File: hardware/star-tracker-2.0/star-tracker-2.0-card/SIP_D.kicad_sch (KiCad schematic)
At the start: 5 parts, among them J6 Conn_01x02, U7 OSD3358-512M-BSM

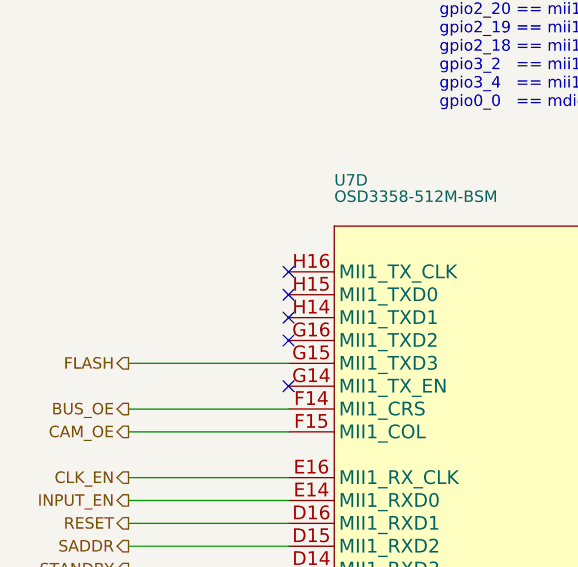
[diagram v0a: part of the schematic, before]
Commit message: Added IMU
added IMU, and i2c pull up resistors to schematic.
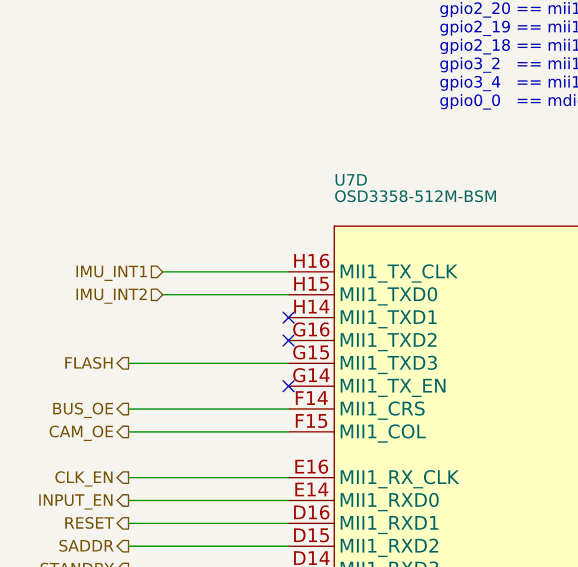
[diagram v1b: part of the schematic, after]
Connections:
- net IMU_INT2: now reaches U7.H15 (MII1_TXD0)
- net IMU_INT1: now reaches U7.H16 (MII1_TX_CLK)
- no-connect marks 20 -> 18
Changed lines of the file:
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@@
-	)
-	(no_connect
-		(at 127 116.84)
 	)
 	(no_connect
@@
 	)
 	(no_connect
-		(at 127 119.38)
-	)
-	(no_connect
 		(at 127 129.54)
 	)
@@
 	(wire
 		(pts
+			(xy 113.03 119.38) (xy 127 119.38)
+		)
+		(stroke
+			(width 0)
+			(type default)
+		)
+	)
+	(wire
+		(pts
 			(xy 213.36 171.45) (xy 213.36 139.7)
 		)
@@
 	(wire
 		(pts
+			(xy 113.03 116.84) (xy 127 116.84)
+		)
+		(stroke
+			(width 0)
+			(type default)
+		)
+	)
+	(wire
+		(pts
 			(xy 187.96 132.08) (xy 238.76 132.08)
 		)
@@
 		(shape output)
 		(at 109.22 142.24 180)
+		(effects
+			(font
+				(size 1.27 1.27)
+			)
+			(justify right)
+		)
+	)
+	(hierarchical_label "IMU_INT2"
+		(shape input)
+		(at 113.03 119.38 180)
 		(effects
 			(font
@@
 		(effects
 			(font
+				(size 1.27 1.27)
+			)
+			(justify right)
+		)
+	)
+	(hierarchical_label "IMU_INT1"
+		(shape input)
+		(at 113.03 116.84 180)
+		(effects
+			(font

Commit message: Routine Push
Updated schematic and layout. about 60% done with routing.
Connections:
- net SYSBOOT2: now also R24.9 (99); no longer R24.8 (88)
- net at R25.1 (11): now also U7.K2 (LCD_DATA10); no longer U7.G3 (LCD_DATA0)
- net at R25.2 (22): now also U7.J3 (LCD_DATA6); no longer U7.G2 (LCD_DATA1)
- net at R25.3 (33): now also U7.J1 (LCD_DATA8)
- net at R25.4 (44): now also U7.G3 (LCD_DATA0); no longer U7.H1 (LCD_DATA5)
- net at R25.6 (66): now also U7.G2 (LCD_DATA1)
- net at R25.7 (77): now also U7.H1 (LCD_DATA5); no longer U7.J3 (LCD_DATA6)
- net at R25.8 (88): now also U7.J2 (LCD_DATA7)
- net at R25.9 (99): now also U7.K1 (LCD_DATA11)
- net at U7.H2 (LCD_DATA4): now also R24.7 (77); no longer R24.6 (66)
- net at U7.H3 (LCD_DATA3): now also R24.8 (88); no longer R24.3 (33)
- net at R26.4 (44): now also U7.K3 (LCD_DATA9); no longer U7.J1 (LCD_DATA8)
- net at R26.6 (66): no longer U7.J2 (LCD_DATA7)
- net at R26.8 (88): no longer U7.K1 (LCD_DATA11)
- net at R26.3 (33): now also U7.L2 (LCD_DATA13); no longer U7.K2 (LCD_DATA10)
- net at R26.7 (77): no longer U7.K3 (LCD_DATA9)
- net at U7.L1 (LCD_DATA14): now also R24.6 (66); no longer R24.4 (44)
- net at R26.9 (99): no longer U7.L2 (LCD_DATA13)

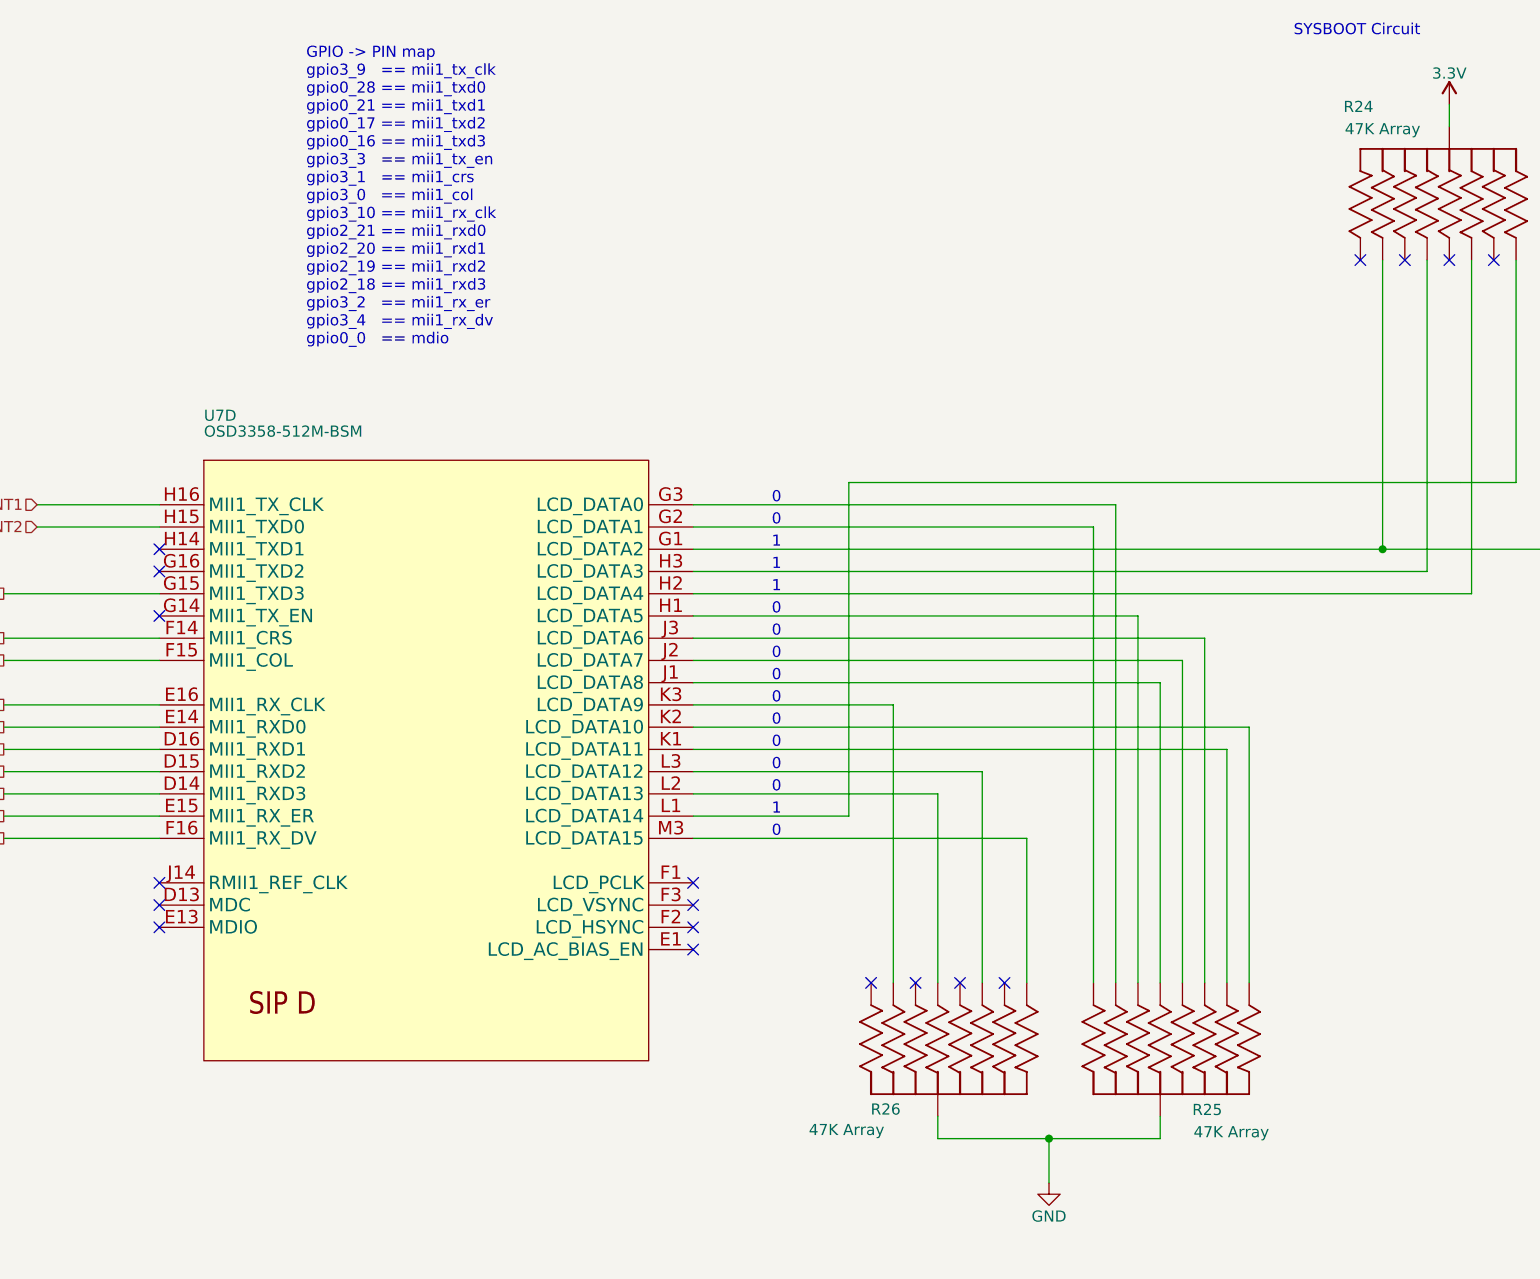
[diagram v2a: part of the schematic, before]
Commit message: Star tracker board update
Added 3d models to footprints, reannotated component designators
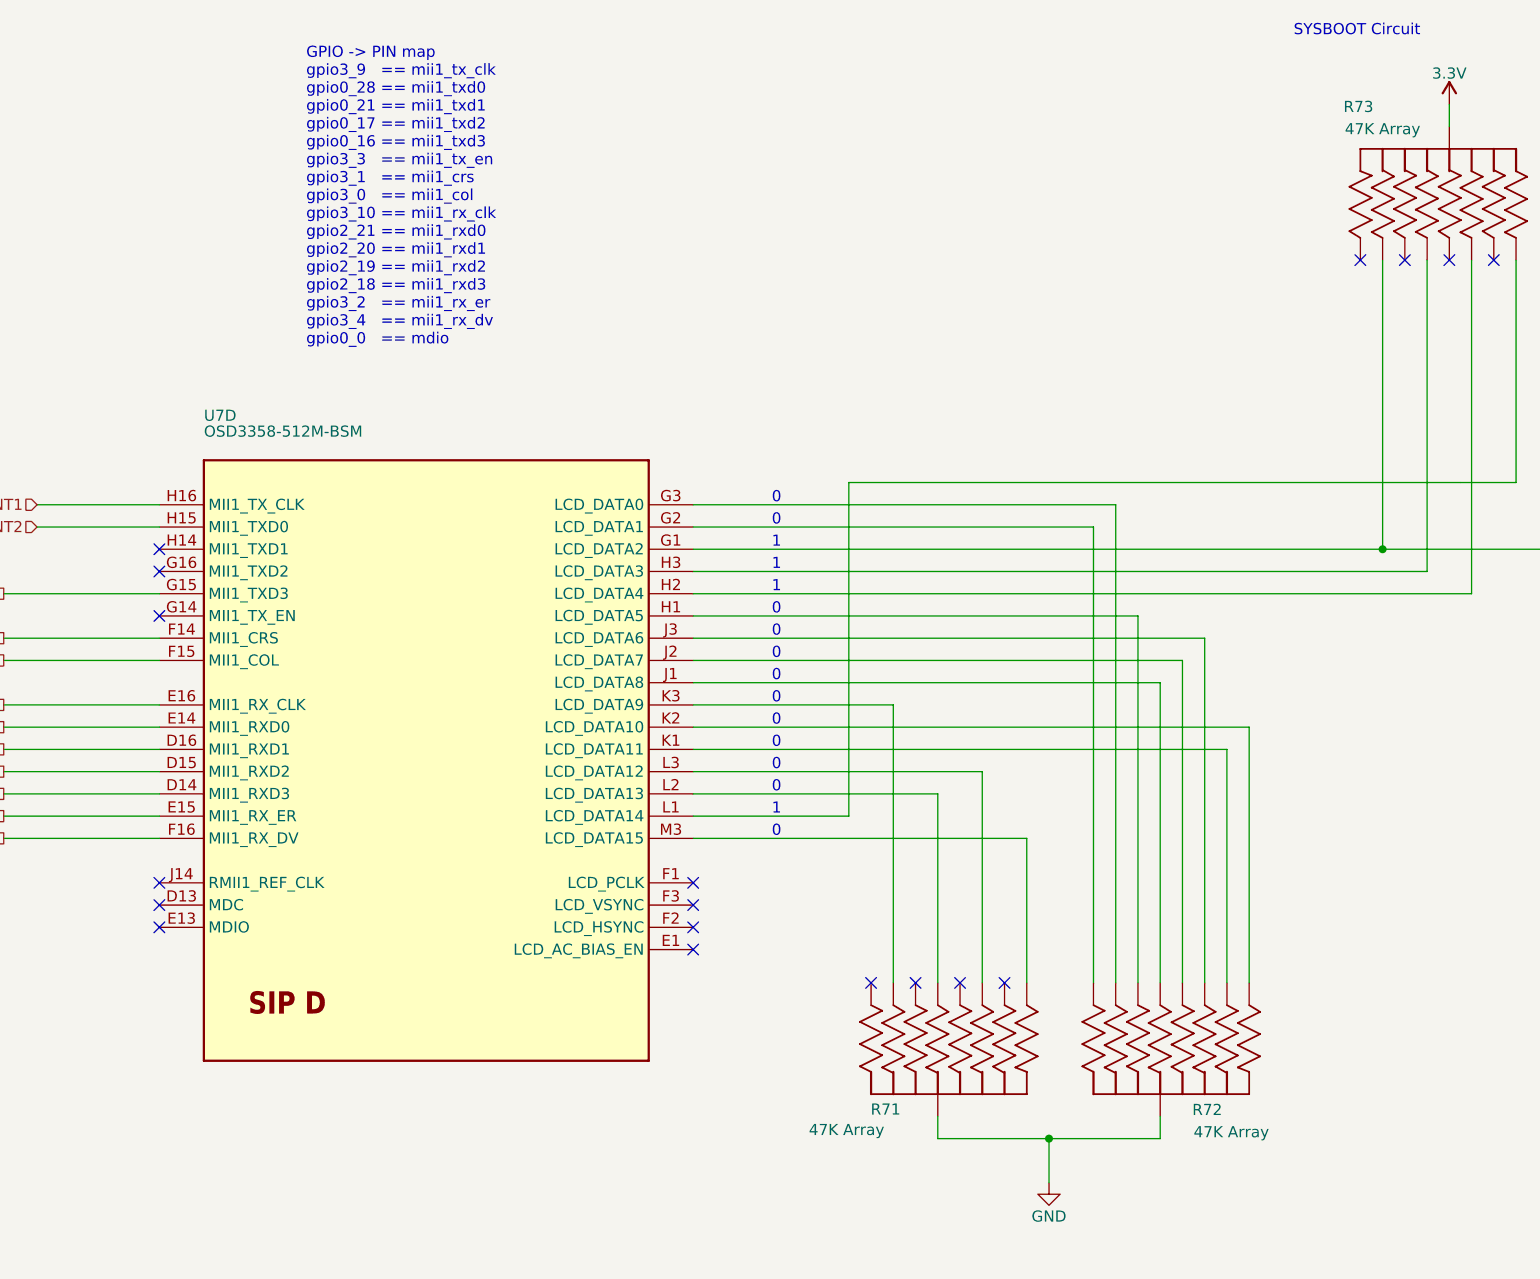
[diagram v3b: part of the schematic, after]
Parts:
- U7: footprint star-tracker-card:OSD335X-BGA-256 -> oresat-ics:U-Octavo-OSD335X-BGA-256; symbol star-tracker-card-eagle-import:OSD3358-512M-BSM -> oresat-ics:OSD3358-512M-BSM; Distributor (none) -> DigiKey; MPN OSD3358-1G-ISM -> OSD3358-512M-BSM
- renumbered R26 to R71, R25 to R72, R24 to R73
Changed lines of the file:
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@@
 	(title_block
 		(title "OreSat Star Tracker")
-		(date "2026-04-22")
-		(rev "1.3")
+		(date "2026-06-05")
+		(rev "2.0")
 		(company "Portland State Aerospace Society")
 	)
@@
 		(in_pos_files yes)
 		(dnp no)
-		(property "Reference" "#PWR51"
+		(property "Reference" "#PWR060"
 			(at 228.6 200.66 0)
 			(hide yes)
@@
 			(project "star-tracker-card"
 				(path "/324e9eb5-7420-4b7e-862c-cc20bb28618a/a084c86d-a957-44c2-8803-b841b67f8737"
-					(reference "#PWR51")
+					(reference "#PWR060")
 					(unit 1)
 				)
@@
 		(in_pos_files yes)
 		(dnp no)
-		(property "Reference" "R25"
+		(property "Reference" "R72"
 			(at 244.9576 186.69 90)
 			(show_name no)
@@
 			(project "star-tracker-card"
 				(path "/324e9eb5-7420-4b7e-862c-cc20bb28618a/a084c86d-a957-44c2-8803-b841b67f8737"
-					(reference "R25")
+					(reference "R72")
 					(unit 1)
 				)
@@
 		(in_pos_files yes)
 		(dnp no)
-		(property "Reference" "#3V-23"
+		(property "Reference" "#3V-016"
 			(at 274.32 68.58 0)
 			(hide yes)
@@
 			(project "star-tracker-card"
 				(path "/324e9eb5-7420-4b7e-862c-cc20bb28618a/a084c86d-a957-44c2-8803-b841b67f8737"
-					(reference "#3V-23")
+					(reference "#3V-016")
 					(unit 1)
 				)
@@
 	)
 	(symbol
-		(lib_id "star-tracker-card-eagle-import:OSD3358-512M-BSM")
+		(lib_id "oresat-ics:OSD3358-512M-BSM")
 		(at 157.48 144.78 0)
 		(unit 4)
@@
 			)
 		)
-		(property "Footprint" "star-tracker-card:OSD335X-BGA-256"
-			(at 157.48 144.78 0)
+		(property "Footprint" "oresat-ics:U-Octavo-OSD335X-BGA-256"
+			(at 157.48 36.83 0)
 			(hide yes)
 			(show_name no)
@@
 			)
 		)
-		(property "Description" "OSD335x Embedded Module ARM® Cortex®-A8, AM3358 1GHz 1GB"
-			(at 157.48 144.78 0)
+		(property "Description" "OSD335x Embedded Module 1GHz 512MB"
+			(at 157.48 40.64 0)
 			(hide yes)
 			(show_name no)
@@
 			)
 		)
-		(property "MPN" "OSD3358-1G-ISM"
-			(at 157.48 144.78 0)
+		(property "MPN" "OSD3358-512M-BSM"
+			(at 157.48 45.72 0)
+			(hide yes)
+			(show_name no)
+			(do_not_autoplace no)
+			(effects
+				(font
+					(size 1.27 1.27)
+				)
+			)
+		)
+		(property "Distributor" "DigiKey"
+			(at 157.48 43.18 0)
 			(hide yes)
 			(show_name no)
@@
 		(in_pos_files yes)
 		(dnp no)
-		(property "Reference" "R26"
+		(property "Reference" "R71"
 			(at 208.2292 186.6392 90)
 			(show_name no)
@@
 			(project "star-tracker-card"
 				(path "/324e9eb5-7420-4b7e-862c-cc20bb28618a/a084c86d-a957-44c2-8803-b841b67f8737"
-					(reference "R26")
+					(reference "R71")
 					(unit 1)
 				)
@@
 		(in_pos_files yes)
 		(dnp no)
-		(property "Reference" "#PWR160"
+		(property "Reference" "#PWR061"
 			(at 298.45 133.35 0)
 			(hide yes)
@@
 			(project "star-tracker-card"
 				(path "/324e9eb5-7420-4b7e-862c-cc20bb28618a/a084c86d-a957-44c2-8803-b841b67f8737"
-					(reference "#PWR160")
+					(reference "#PWR061")
 					(unit 1)
 				)
@@
 		(in_pos_files yes)
 		(dnp no)
-		(property "Reference" "R24"
+		(property "Reference" "R73"
 			(at 262.2296 72.136 90)
 			(show_name no)
@@
 			(project "star-tracker-card"
 				(path "/324e9eb5-7420-4b7e-862c-cc20bb28618a/a084c86d-a957-44c2-8803-b841b67f8737"
-					(reference "R24")
+					(reference "R73")
 					(unit 1)
 				)

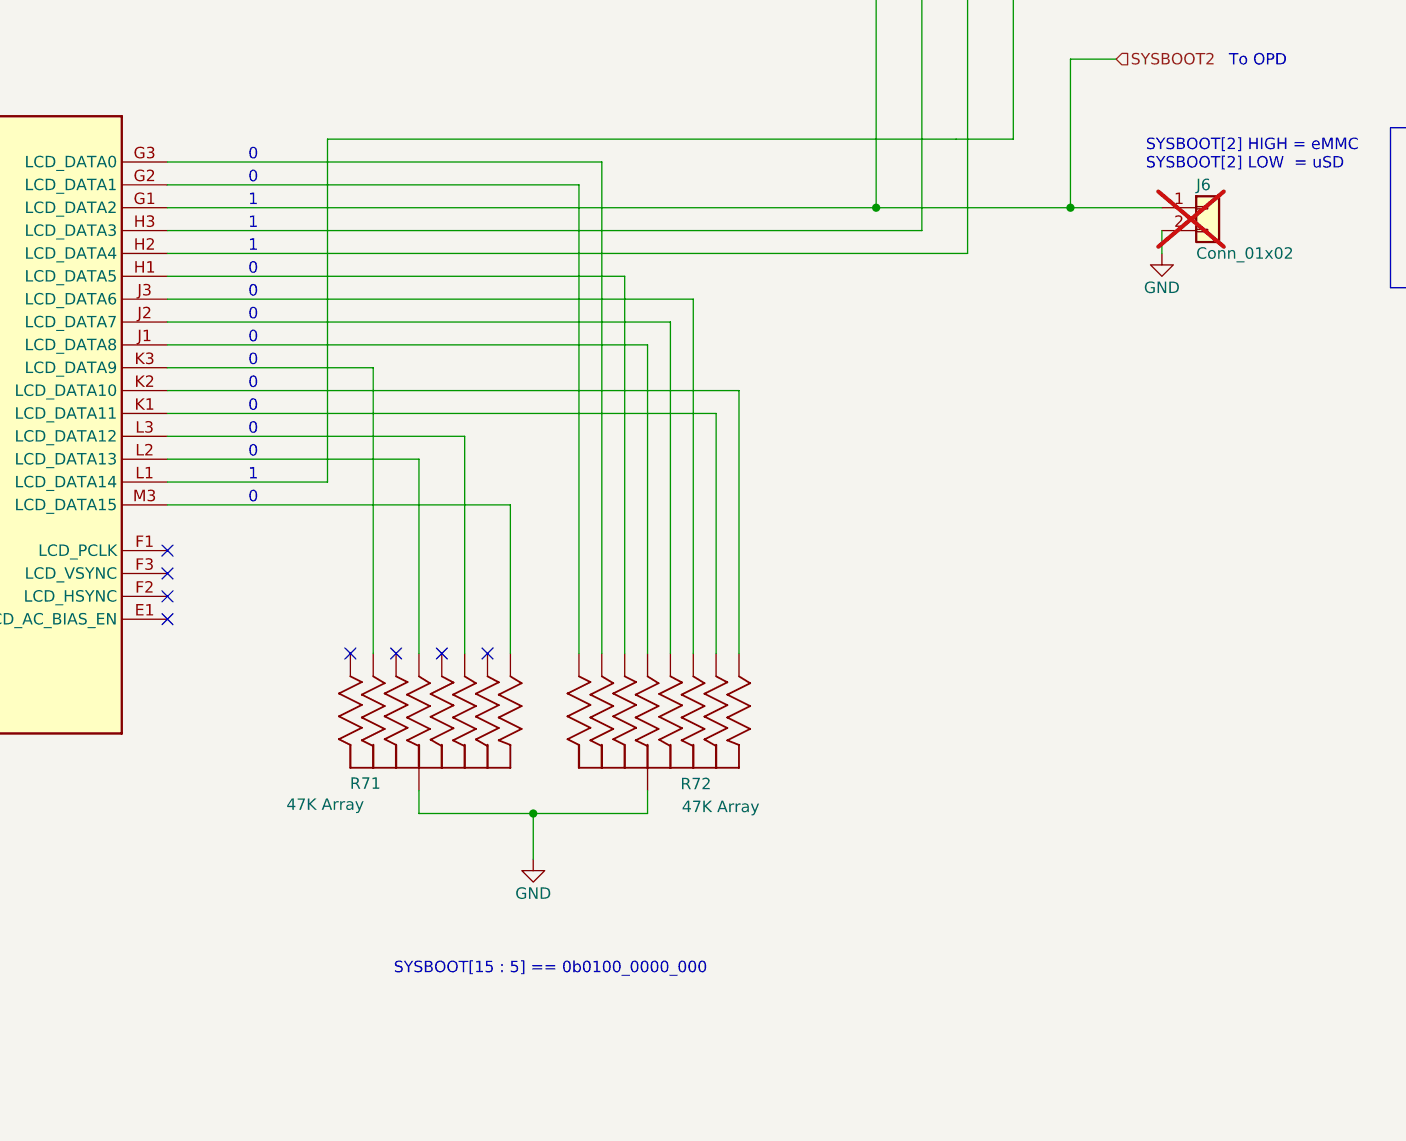
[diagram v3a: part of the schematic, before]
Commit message: Added pull up and pull down resistors
aded PU and PD resistors for firmware revision set.
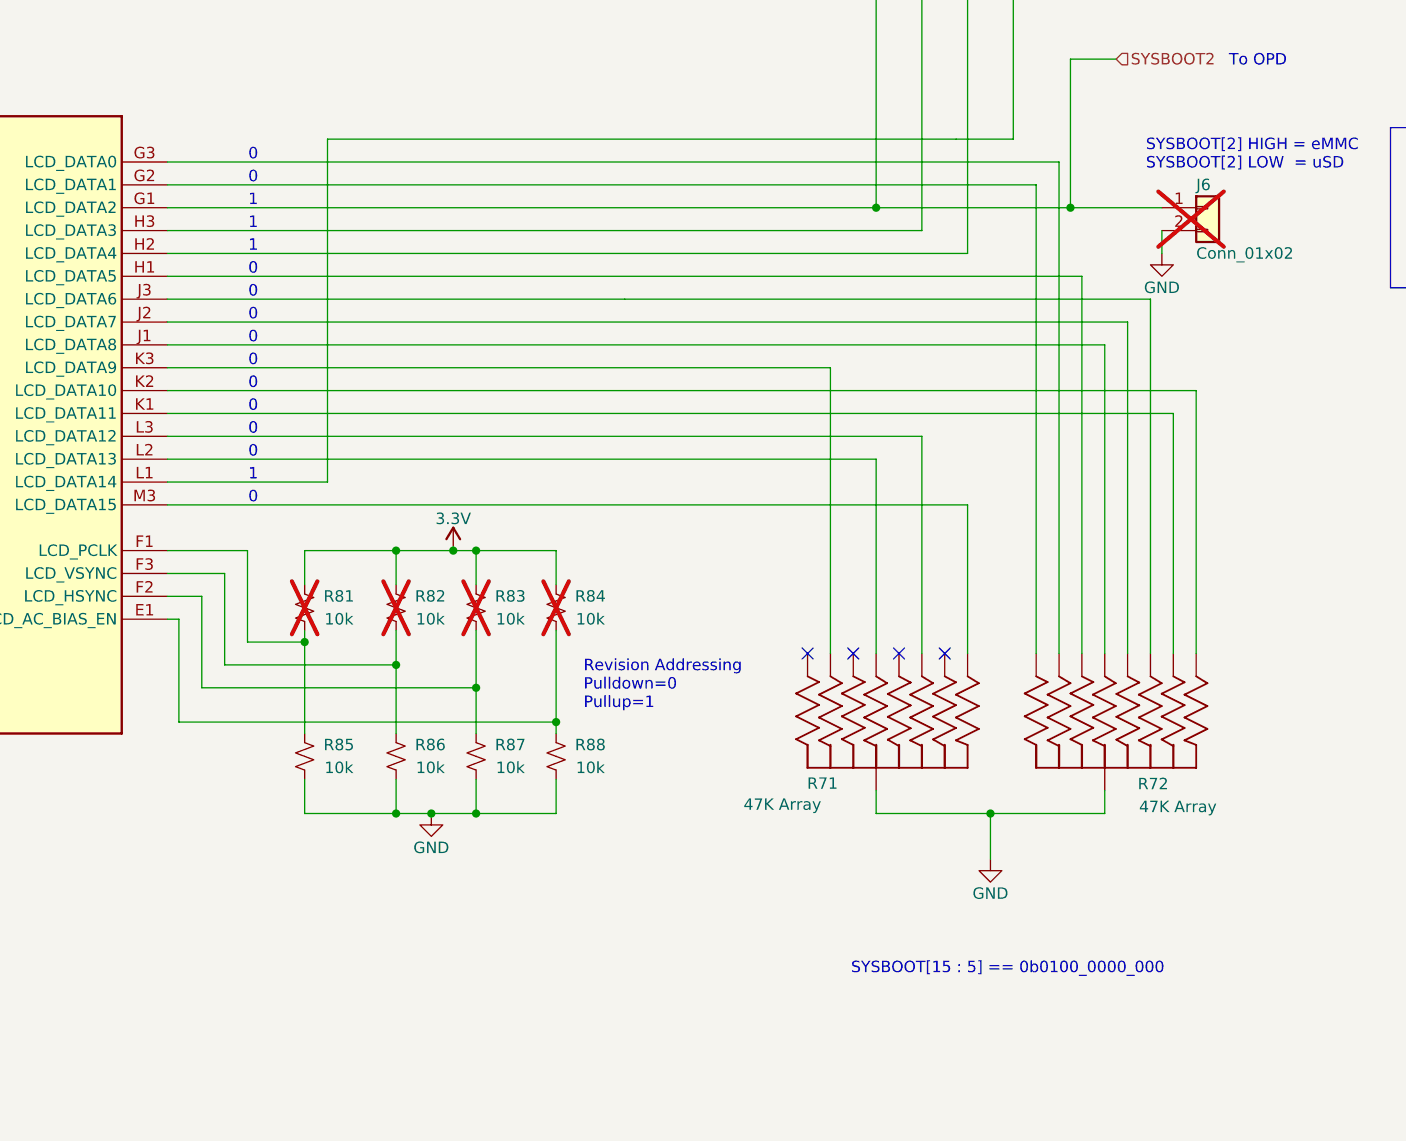
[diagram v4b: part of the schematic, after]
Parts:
- added R81, R82, R83, R84, R85, R86, R87, R88: 10k, oresat-passives:0603-C-NOSILK, symbol Device:R_Small_US
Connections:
- net 3.3V: now also R81.2, R82.2, R83.2, R84.2
- net GND: now also R85.1, R86.1, R87.1, R88.1
- net at U7.E1 (LCD_AC_BIAS_EN): now also R84.1, R88.2
- net at U7.F1 (LCD_PCLK): now also R81.1, R85.2
- net at U7.F2 (LCD_HSYNC): now also R83.1, R87.2
- net at U7.F3 (LCD_VSYNC): now also R82.1, R86.2
- no-connect marks 18 -> 14
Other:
- note added: "Revision Addressing Pulldown=0 Pullup=1"
- moved on the sheet: R71, R72
